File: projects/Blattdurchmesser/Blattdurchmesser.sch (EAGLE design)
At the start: 16 parts, among them K1 TX2_RELAY", Q1 ARDUINOR3-NOIOREF-NOTEXT

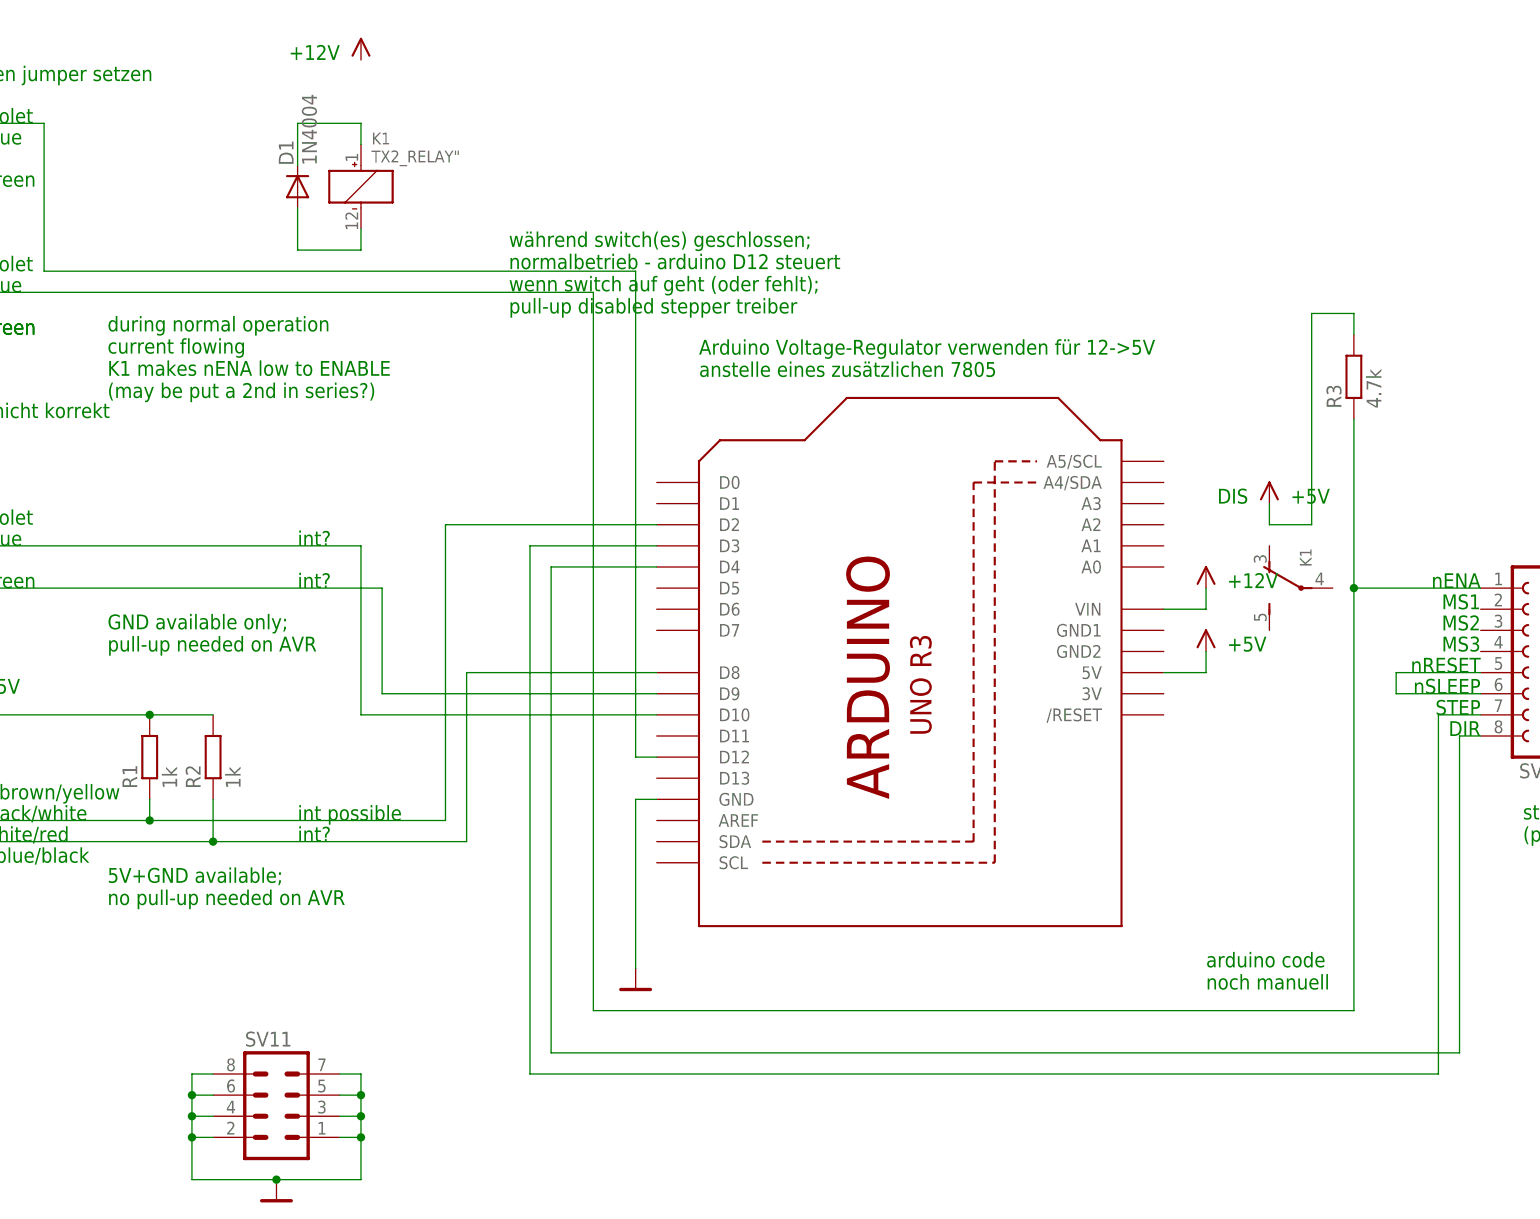
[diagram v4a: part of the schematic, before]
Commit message: new feature; * add i2c OLED display
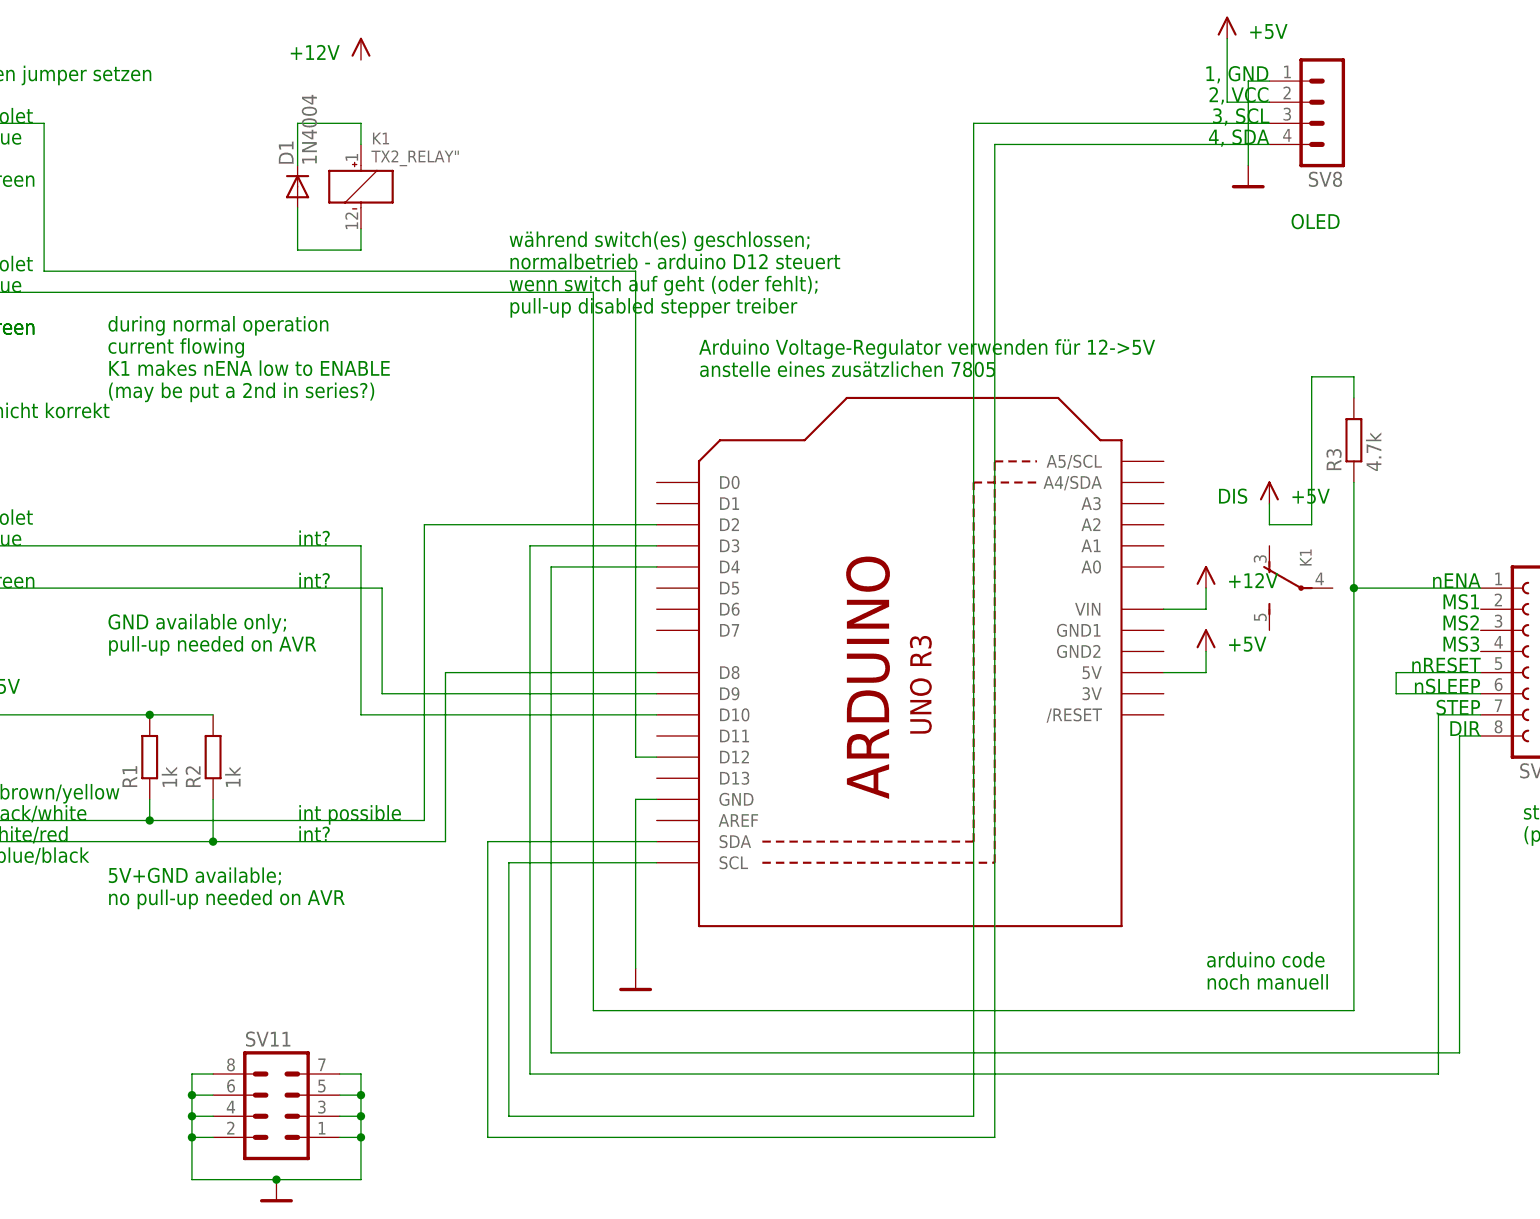
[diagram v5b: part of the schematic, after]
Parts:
- added SV8: (no value), con-lstb:MA04-1
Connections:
- new net N$17: Q1.SCL, SV8.3
- new net N$18: Q1.SDA, SV8.4
- net +5V: now also SV8.2
- net GND: now also SV8.1
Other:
- note added: "1, GND"
- note added: "2, VCC"
- note added: "3, SCL"
- note added: "4, SDA"
- note added: "OLED"
- moved on the sheet: R3
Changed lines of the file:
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@@
 <part name="X1" library="con-wago-508" deviceset="W237-02P" device=""/>
 <part name="U$2" library="Netze" deviceset="+12V" device=""/>
+<part name="SV8" library="con-lstb" deviceset="MA04-1" device=""/>
+<part name="U$12" library="Netze" deviceset="GND" device=""/>
+<part name="U$14" library="Netze" deviceset="+5V" device=""/>
 </parts>
 <sheets>
@@
 <text x="58.42" y="71.12" size="1.778" layer="91">Arduino Voltage-Regulator verwenden für 12-&gt;5V
 anstelle eines zusätzlichen 7805</text>
+<text x="127" y="106.68" size="1.778" layer="91" rot="MR0">1, GND</text>
+<text x="127" y="104.14" size="1.778" layer="91" rot="MR0">2, VCC</text>
+<text x="127" y="101.6" size="1.778" layer="91" rot="MR0">3, SCL</text>
+<text x="127" y="99.06" size="1.778" layer="91" rot="MR0">4, SDA</text>
+<text x="124.46" y="111.76" size="1.778" layer="91">+5V</text>
+<text x="129.54" y="88.9" size="1.778" layer="91">OLED</text>
 </plain>
 <instances>
@@
 <instance part="U$13" gate="1" x="17.78" y="104.14"/>
 <instance part="D1" gate="1" x="10.16" y="93.98" rot="R90"/>
-<instance part="R3" gate="G$1" x="137.16" y="71.12" rot="R90"/>
+<instance part="R3" gate="G$1" x="137.16" y="63.5" rot="R90"/>
 <instance part="Q1" gate="G$1" x="83.82" y="38.1" rot="R90"/>
 <instance part="SV7" gate="1" x="-38.1" y="96.52" rot="MR180"/>
@@
 <instance part="X1" gate="-2" x="175.26" y="2.54"/>
 <instance part="U$2" gate="1" x="119.38" y="40.64"/>
+<instance part="SV8" gate="1" x="134.62" y="101.6" rot="R180"/>
+<instance part="U$12" gate="1" x="124.46" y="96.52"/>
+<instance part="U$14" gate="1" x="121.92" y="111.76"/>
 </instances>
 <busses>
@@
 <junction x="7.62" y="-25.4"/>
 </segment>
+<segment>
+<pinref part="U$12" gate="1" pin="GND"/>
+<wire x1="124.46" y1="96.52" x2="124.46" y2="106.68" width="0.1524" layer="91"/>
+<pinref part="SV8" gate="1" pin="1"/>
+<wire x1="124.46" y1="106.68" x2="127" y2="106.68" width="0.1524" layer="91"/>
+</segment>
 </net>
 <net name="+5V" class="0">
@@
 <wire x1="127" y1="55.88" x2="127" y2="53.34" width="0.1524" layer="91"/>
 <wire x1="127" y1="53.34" x2="132.08" y2="53.34" width="0.1524" layer="91"/>
-<wire x1="132.08" y1="53.34" x2="132.08" y2="78.74" width="0.1524" layer="91"/>
+<wire x1="132.08" y1="53.34" x2="132.08" y2="71.12" width="0.1524" layer="91"/>
 <pinref part="R3" gate="G$1" pin="2"/>
-<wire x1="132.08" y1="78.74" x2="137.16" y2="78.74" width="0.1524" layer="91"/>
-<wire x1="137.16" y1="78.74" x2="137.16" y2="76.2" width="0.1524" layer="91"/>
+<wire x1="132.08" y1="71.12" x2="137.16" y2="71.12" width="0.1524" layer="91"/>
+<wire x1="137.16" y1="71.12" x2="137.16" y2="68.58" width="0.1524" layer="91"/>
+</segment>
+<segment>
+<pinref part="SV8" gate="1" pin="2"/>
+<pinref part="U$14" gate="1" pin="+5V"/>
+<wire x1="127" y1="104.14" x2="121.92" y2="104.14" width="0.1524" layer="91"/>
+<wire x1="121.92" y1="104.14" x2="121.92" y2="111.76" width="0.1524" layer="91"/>
 </segment>
 </net>
@@
 <wire x1="0" y1="15.24" x2="0" y2="20.32" width="0.1524" layer="91"/>
 <junction x="0" y="15.24"/>
-<wire x1="0" y1="15.24" x2="30.48" y2="15.24" width="0.1524" layer="91"/>
-<wire x1="30.48" y1="15.24" x2="30.48" y2="35.56" width="0.1524" layer="91"/>
-<wire x1="30.48" y1="35.56" x2="53.34" y2="35.56" width="0.1524" layer="91"/>
+<wire x1="0" y1="15.24" x2="27.94" y2="15.24" width="0.1524" layer="91"/>
+<wire x1="27.94" y1="15.24" x2="27.94" y2="35.56" width="0.1524" layer="91"/>
+<wire x1="27.94" y1="35.56" x2="53.34" y2="35.56" width="0.1524" layer="91"/>
 <pinref part="Q1" gate="G$1" pin="D8"/>
 </segment>
@@
 <wire x1="152.4" y1="45.72" x2="137.16" y2="45.72" width="0.1524" layer="91"/>
 <pinref part="R3" gate="G$1" pin="1"/>
-<wire x1="137.16" y1="66.04" x2="137.16" y2="45.72" width="0.1524" layer="91"/>
+<wire x1="137.16" y1="58.42" x2="137.16" y2="45.72" width="0.1524" layer="91"/>
 <junction x="137.16" y="45.72"/>
 </segment>
@@
 <pinref part="R1" gate="G$1" pin="1"/>
 <wire x1="-7.62" y1="17.78" x2="-7.62" y2="20.32" width="0.1524" layer="91"/>
-<wire x1="27.94" y1="17.78" x2="27.94" y2="53.34" width="0.1524" layer="91"/>
-<wire x1="27.94" y1="53.34" x2="53.34" y2="53.34" width="0.1524" layer="91"/>
-<wire x1="-7.62" y1="17.78" x2="27.94" y2="17.78" width="0.1524" layer="91"/>
+<wire x1="25.4" y1="17.78" x2="25.4" y2="53.34" width="0.1524" layer="91"/>
+<wire x1="25.4" y1="53.34" x2="53.34" y2="53.34" width="0.1524" layer="91"/>
+<wire x1="-7.62" y1="17.78" x2="25.4" y2="17.78" width="0.1524" layer="91"/>
 <junction x="-7.62" y="17.78"/>
 <pinref part="Q1" gate="G$1" pin="D2"/>
@@
 </segment>
 </net>
+<net name="N$17" class="0">
+<segment>
+<pinref part="SV8" gate="1" pin="3"/>
+<wire x1="91.44" y1="101.6" x2="127" y2="101.6" width="0.1524" layer="91"/>
+<wire x1="91.44" y1="101.6" x2="91.44" y2="-17.78" width="0.1524" layer="91"/>
+<wire x1="91.44" y1="-17.78" x2="35.56" y2="-17.78" width="0.1524" layer="91"/>
+<wire x1="35.56" y1="-17.78" x2="35.56" y2="12.7" width="0.1524" layer="91"/>
+<pinref part="Q1" gate="G$1" pin="SCL"/>
+<wire x1="35.56" y1="12.7" x2="53.34" y2="12.7" width="0.1524" layer="91"/>
+</segment>
+</net>
+<net name="N$18" class="0">
+<segment>
+<pinref part="SV8" gate="1" pin="4"/>
+<wire x1="127" y1="99.06" x2="93.98" y2="99.06" width="0.1524" layer="91"/>
+<wire x1="93.98" y1="99.06" x2="93.98" y2="-20.32" width="0.1524" layer="91"/>
+<wire x1="93.98" y1="-20.32" x2="33.02" y2="-20.32" width="0.1524" layer="91"/>
+<wire x1="33.02" y1="-20.32" x2="33.02" y2="15.24" width="0.1524" layer="91"/>
+<pinref part="Q1" gate="G$1" pin="SDA"/>
+<wire x1="53.34" y1="15.24" x2="33.02" y2="15.24" width="0.1524" layer="91"/>
+</segment>
+</net>

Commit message: improvement; * rearranged schematic              * rearranged pcb
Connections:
- net N$15: now also Q1.A0
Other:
- note added: "use JUMPER to ignore during normal operation: signal Arduino D12 passed through to nENA otherwise: nENA pulled up to DISABLE"
- note removed: "during normal operation current flowing K1 makes nENA low to ENABLE (may be put a 2nd in series?)"
- note removed: "wenn nicht vorhanden jumper setzen"
- note removed: "während switch(es) geschlossen; normalbetrieb - arduino D12 steuert wenn switch auf geht (oder fehlt); pull-up disabled stepper treiber"
- moved on the sheet: C1, D1, K1, R1, R2, R3, SV1, SV11, SV2, SV3, SV4, SV5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

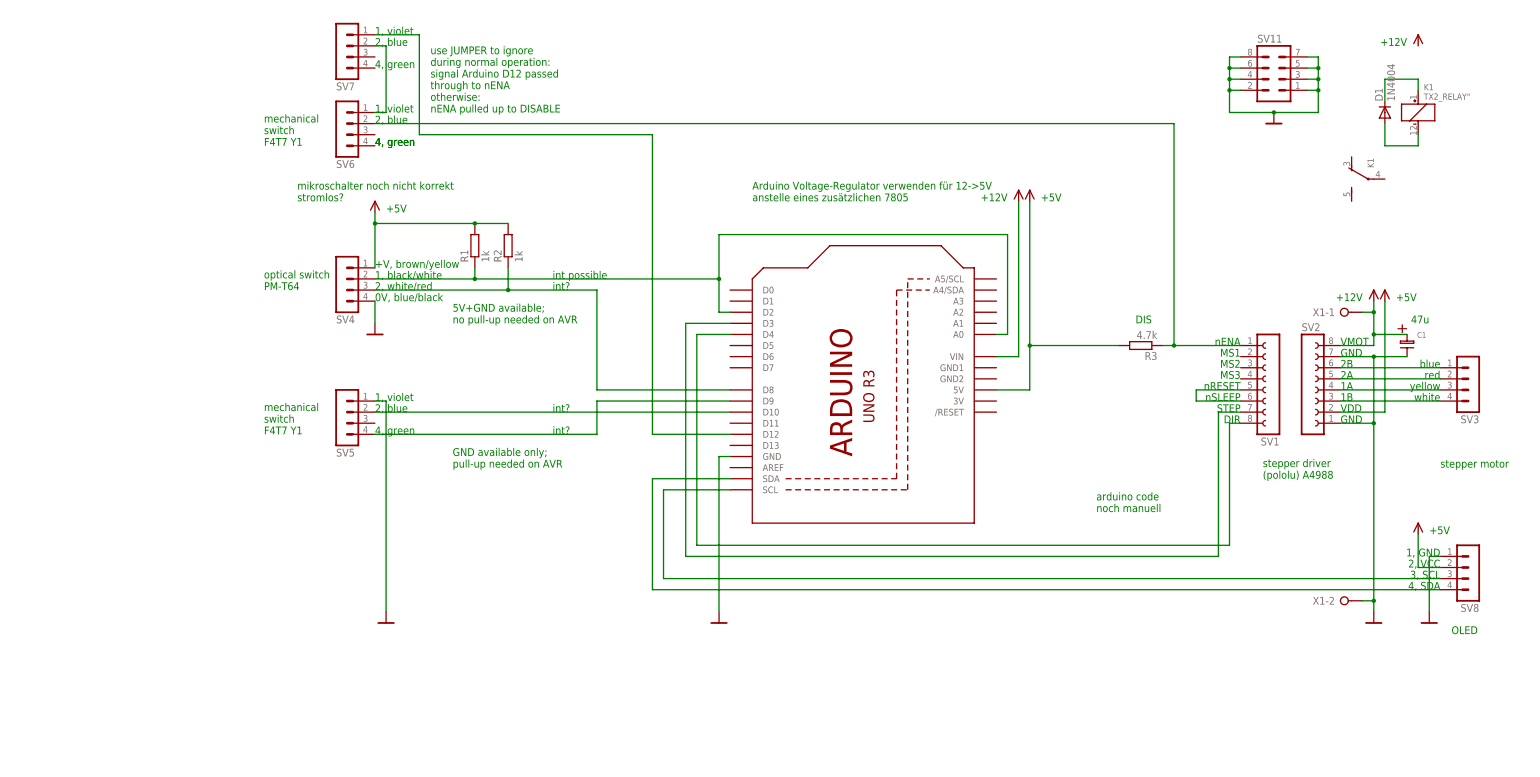
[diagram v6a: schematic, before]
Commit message: improvement; * move stepper power line to top plane              * add labels to connectors
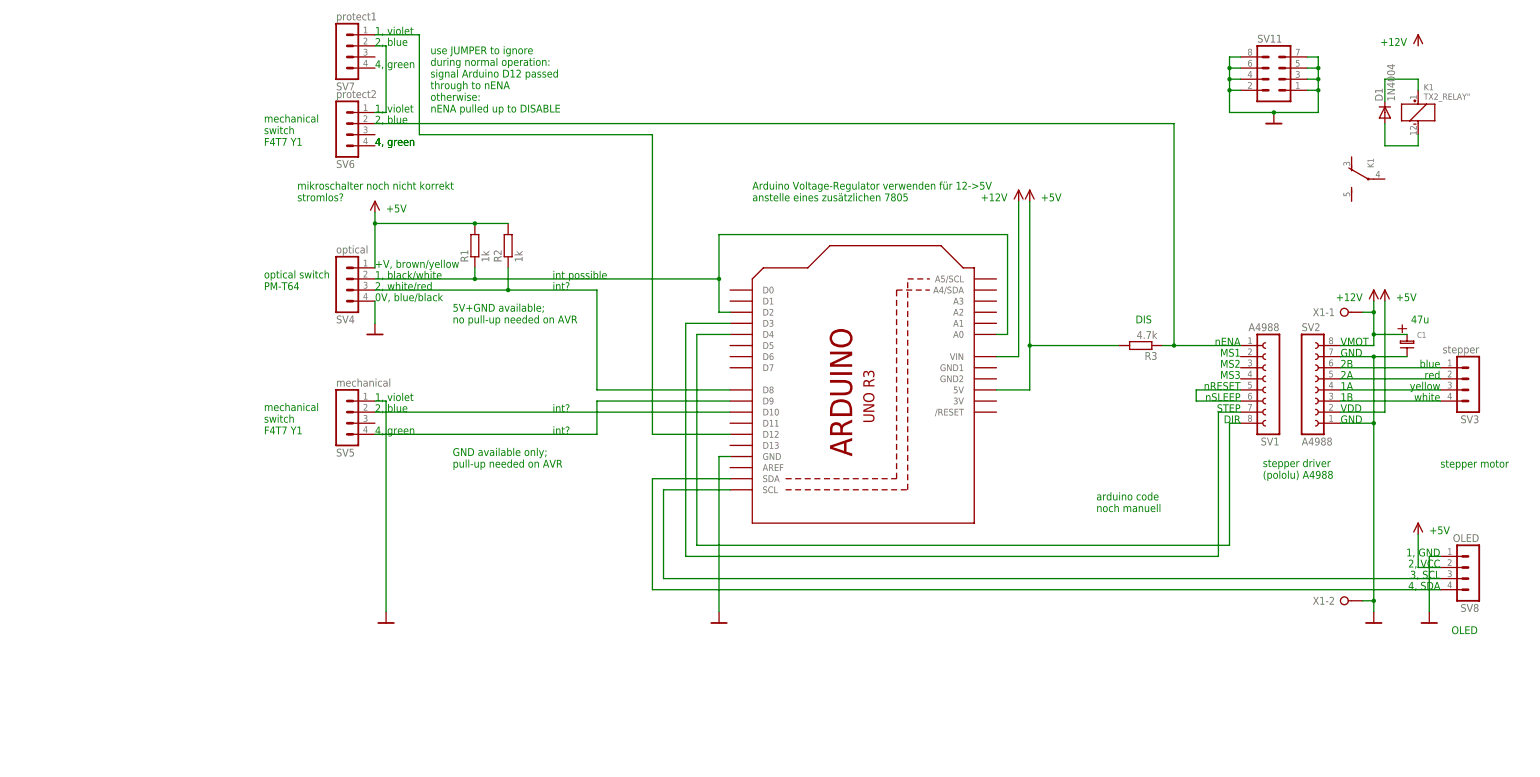
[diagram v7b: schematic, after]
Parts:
- SV1, SV2: value (none) -> A4988
- SV3: value (none) -> stepper
- SV4: value (none) -> optical
- SV5: value (none) -> mechanical
- SV6: value (none) -> protect2
- SV7: value (none) -> protect1
- SV8: value (none) -> OLED
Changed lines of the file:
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@@
 <parts>
 <part name="K1" library="relay" deviceset="TX2_RELAY" device="&quot;"/>
-<part name="SV1" library="con-lsta" deviceset="FE08-1" device=""/>
-<part name="SV2" library="con-lsta" deviceset="FE08-1" device=""/>
-<part name="SV4" library="con-lstb" deviceset="MA04-1" device=""/>
+<part name="SV1" library="con-lsta" deviceset="FE08-1" device="" value="A4988"/>
+<part name="SV2" library="con-lsta" deviceset="FE08-1" device="" value="A4988"/>
+<part name="SV4" library="con-lstb" deviceset="MA04-1" device="" value="optical"/>
 <part name="SV11" library="con-lstb" deviceset="MA04-2" device=""/>
 <part name="U$1" library="Netze" deviceset="GND" device=""/>
@@
 <part name="U$5" library="Netze" deviceset="+5V" device=""/>
 <part name="U$6" library="Netze" deviceset="+12V" device=""/>
-<part name="SV3" library="con-lstb" deviceset="MA04-1" device=""/>
+<part name="SV3" library="con-lstb" deviceset="MA04-1" device="" value="stepper"/>
 <part name="U$7" library="Netze" deviceset="+5V" device=""/>
 <part name="C1" library="Elkos" deviceset="R_ELKO_8.1" device=""/>
-<part name="SV5" library="con-lstb" deviceset="MA04-1" device=""/>
+<part name="SV5" library="con-lstb" deviceset="MA04-1" device="" value="mechanical"/>
 <part name="R1" library="rcl" deviceset="R-EU_" device="0207/10" value="1k"/>
 <part name="R2" library="rcl" deviceset="R-EU_" device="0207/10" value="1k"/>
@@
 <part name="U$10" library="Netze" deviceset="GND" device=""/>
 <part name="U$11" library="Netze" deviceset="GND" device=""/>
-<part name="SV6" library="con-lstb" deviceset="MA04-1" device=""/>
+<part name="SV6" library="con-lstb" deviceset="MA04-1" device="" value="protect2"/>
 <part name="U$13" library="Netze" deviceset="+12V" device=""/>
 <part name="D1" library="diode" deviceset="1N4004" device=""/>
 <part name="R3" library="rcl" deviceset="R-EU_" device="0207/10" value="4.7k"/>
 <part name="Q1" library="adafruit" deviceset="ARDUINOR3-NOIOREF" device="-NOTEXT"/>
-<part name="SV7" library="con-lstb" deviceset="MA04-1" device=""/>
+<part name="SV7" library="con-lstb" deviceset="MA04-1" device="" value="protect1"/>
 <part name="X1" library="con-wago-508" deviceset="W237-02P" device=""/>
 <part name="U$2" library="Netze" deviceset="+12V" device=""/>
-<part name="SV8" library="con-lstb" deviceset="MA04-1" device=""/>
+<part name="SV8" library="con-lstb" deviceset="MA04-1" device="" value="OLED"/>
 <part name="U$12" library="Netze" deviceset="GND" device=""/>
 <part name="U$14" library="Netze" deviceset="+5V" device=""/>
